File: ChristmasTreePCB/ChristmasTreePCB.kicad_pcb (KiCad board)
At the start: 2 copper layers, 17 parts, among them J1 ICSP, U1 ATtiny85-20SHR

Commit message: Rough layout
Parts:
- added H1: M2, MountingHole:MountingHole_2.1mm, F.Cu at (232.4, 28.4)
- added SW1: SPST-NO, Button_Switch_SMD:SW_SPST_PTS645, F.Cu at (232.4, 102.2)
- BT1: moved to B.Cu
- D2, D5: value LED -> Green
- D3, D6: value LED -> Blue
- D4, D7: value LED -> Red
- moved BT1 140.9 mm to (238.7, 102.8)
- moved D2 132.6 mm to (262.0, 86.0), turned to 180 degrees
- moved D4 129.1 mm to (245.0, 44.0), turned to 180 degrees
- moved R3 126.3 mm to (261.2, 96.9)
- moved D6 124.1 mm to (253.1, 64.9), turned to 180 degrees
- moved D1 123.2 mm to (232.4, 32.2)
- moved R6 119.0 mm to (254.4, 99.2)
- moved J1 107.1 mm to (231.1, 110.7)
- moved D3 102.4 mm to (219.6, 43.8)
- moved C1 102.1 mm to (238.9, 76.8), turned to 90 degrees
- moved R4 102.1 mm to (246.5, 101.2)
- moved U1 95.0 mm to (232.0, 78.1)
- moved R1 78.7 mm to (209.4, 100.7)
- moved D5 77.6 mm to (211.3, 64.6)
- moved R5 76.9 mm to (216.9, 101.2)
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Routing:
- added copper zone on B.Cu, net GND
- added copper zone on F.Cu, net GND
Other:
- board outline added: 87 x 93.9 mm
- net class Default: trace_width 0.25 -> 0.254

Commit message: 50% complete routing
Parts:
- BT1: footprint Battery:BatteryHolder_Keystone_2468_2xAAA -> ChristmasTreeCustomFootprints:2468_Custom
- moved R6 9.17 mm to (245.2, 99.8)
- moved R4 7.38 mm to (252.6, 97.0)
- moved BT1 7.01 mm to (245.1, 105.8)
- moved R2 5.19 mm to (204.8, 94.4)
- moved R1 4.62 mm to (212.4, 97.1), turned to 180 degrees
- moved R5 3.30 mm to (219.9, 99.8), turned to 180 degrees
- moved R3 3.04 mm to (259.9, 94.1), turned to 180 degrees
- moved C1 1.18 mm to (238.1, 77.7)
- moved U1 0.93 mm to (232.4, 78.9)
- moved D4 0.72 mm to (244.5, 43.5)
- moved D3 0.71 mm to (220.3, 43.5)
- moved SW1 0.54 mm to (232.4, 102.8)
- moved D2 0.45 mm to (261.7, 85.6)
- moved D7 0.36 mm to (203.0, 85.6)
- moved D6 0.30 mm to (253.1, 64.6)
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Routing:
- net Net-(D2-Pad2): track 0.00 -> 102.7 mm
- net PB0-MOSI-RED: track 0.00 -> 79.6 mm, vias 0 -> 2
- net PB1-MISO-GREEN: track 0.00 -> 62.0 mm
- net VCC: track 0.00 -> 59.6 mm
- net PB2-SCK-BLUE: track 0.00 -> 55.2 mm, vias 0 -> 2
- net PCINT3: track 0.00 -> 41.9 mm, vias 0 -> 2
- net RESET: track 0.00 -> 35.5 mm
- net Net-(D2-Pad1): track 0.00 -> 18.0 mm
- net GND: vias 0 -> 11
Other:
- board text added: "Sherstans 2021"

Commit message: roting complete
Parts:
- moved D1 0.50 mm to (232.4, 31.7)
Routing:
- net Net-(D3-Pad2): track 0.00 -> 142.7 mm, vias 0 -> 2
- net Net-(D2-Pad1): track 18.0 -> 151.9 mm, vias 0 -> 2
- net Net-(D1-Pad2): track 0.00 -> 84.1 mm, vias 0 -> 2
- net PB4-WHITE: track 0.00 -> 44.9 mm, vias 0 -> 2
- net RESET: track 35.5 -> 72.9 mm, vias 0 -> 2
- net Net-(D2-Pad2): track 102.7 -> 132.6 mm, vias 0 -> 2
- net VCC: track 59.6 -> 82.7 mm, vias 0 -> 2
- net GND: vias 11 -> 21

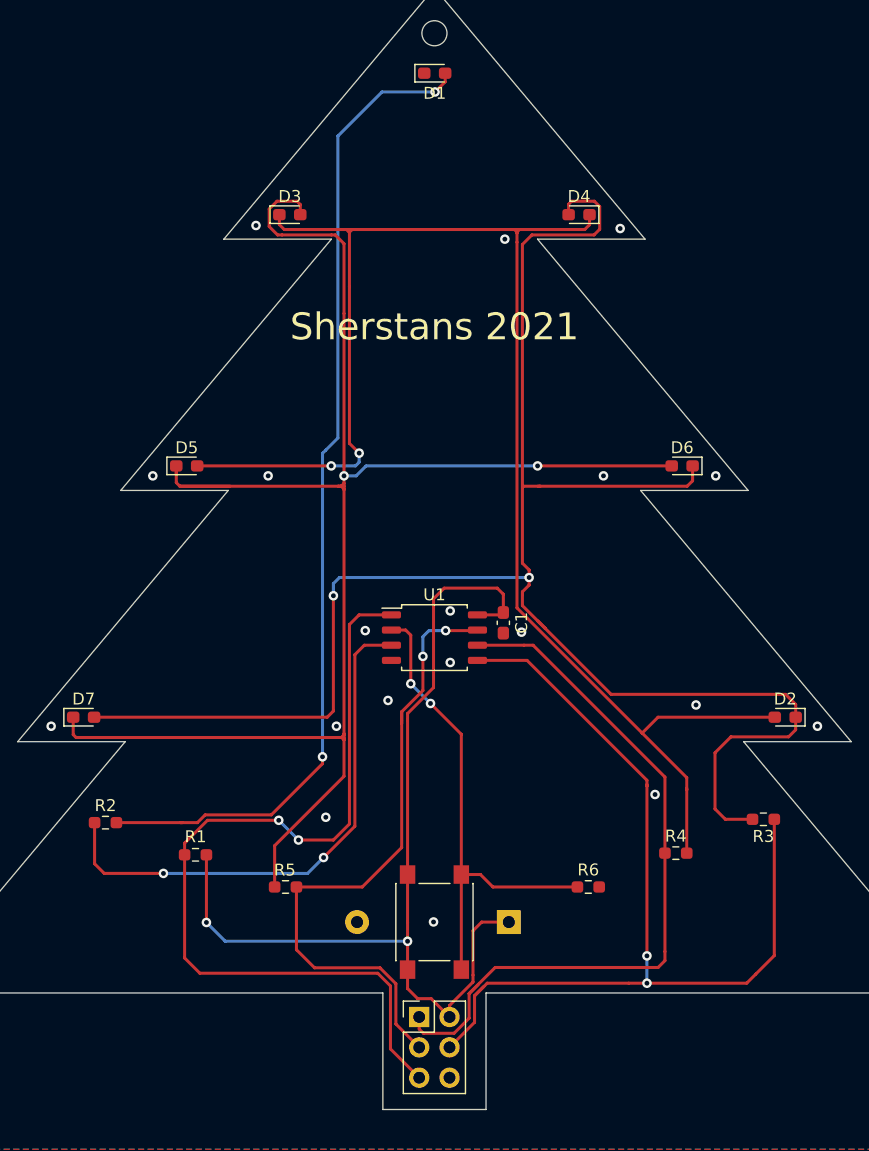
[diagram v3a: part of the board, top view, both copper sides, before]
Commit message: Clean up routing
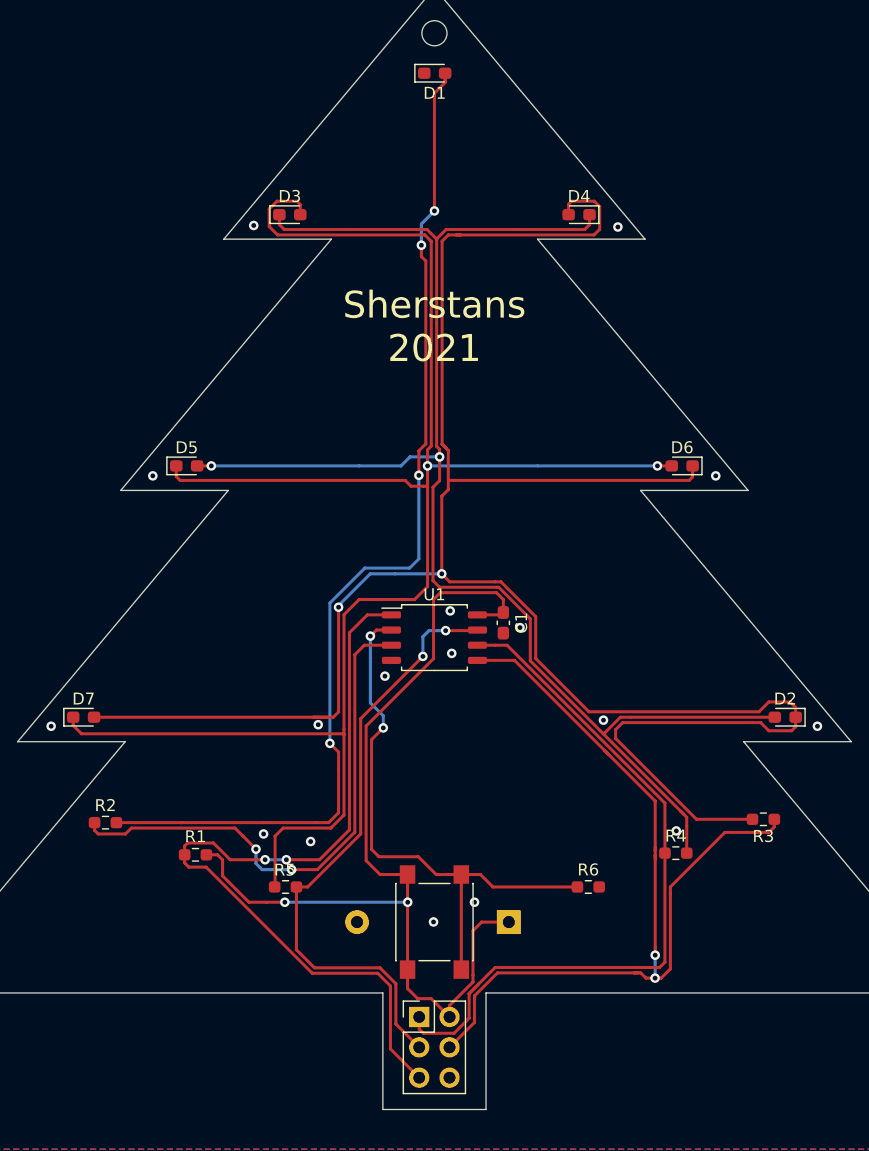
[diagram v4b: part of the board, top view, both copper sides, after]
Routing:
- net Net-(D2-Pad1): track 151.9 -> 179.6 mm
- net Net-(D3-Pad2): track 142.7 -> 150.5 mm
- net PCINT3: track 41.9 -> 47.2 mm
- net RESET: track 72.9 -> 67.7 mm
- net Net-(D1-Pad2): track 84.1 -> 88.7 mm, vias 2 -> 4
- net PB2-SCK-BLUE: track 55.2 -> 51.6 mm
- net Net-(D2-Pad2): track 132.6 -> 129.4 mm
- net PB0-MOSI-RED: track 79.6 -> 77.7 mm
- net PB1-MISO-GREEN: track 62.2 -> 61.0 mm
- net GND: vias 21 -> 19

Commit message: Pre save before gerbers
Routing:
- net RESET: track 67.7 -> 72.1 mm, vias 2 -> 0
- net PB4-WHITE: track 44.4 -> 41.9 mm
- net PCINT3: track 47.2 -> 45.4 mm
- net VCC: track 82.7 -> 84.1 mm
- net PB2-SCK-BLUE: track 51.6 -> 50.2 mm
- net PB0-MOSI-RED: track 77.7 -> 78.5 mm
- net Net-(D2-Pad2): track 129.4 -> 130.2 mm
- net Net-(D3-Pad2): track 150.5 -> 149.9 mm
- net GND: vias 19 -> 17
